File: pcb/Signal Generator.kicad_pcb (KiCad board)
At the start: 2 copper layers, 50 parts, among them J1 USB_C_Receptacle_USB2.0, J2 AudioJack3, J3 Conn_02x02_Odd_Even, J4 Screw_Terminal_01x04, SW1 SW_Push, SW2 SW_SPDT, U1 FT230XQ, U2 Opamp_Dual, U3 STM32F071RBTx, U4 LD39050PU33R, Y1 TG2520SMN_16.0000M-MCGNNM0

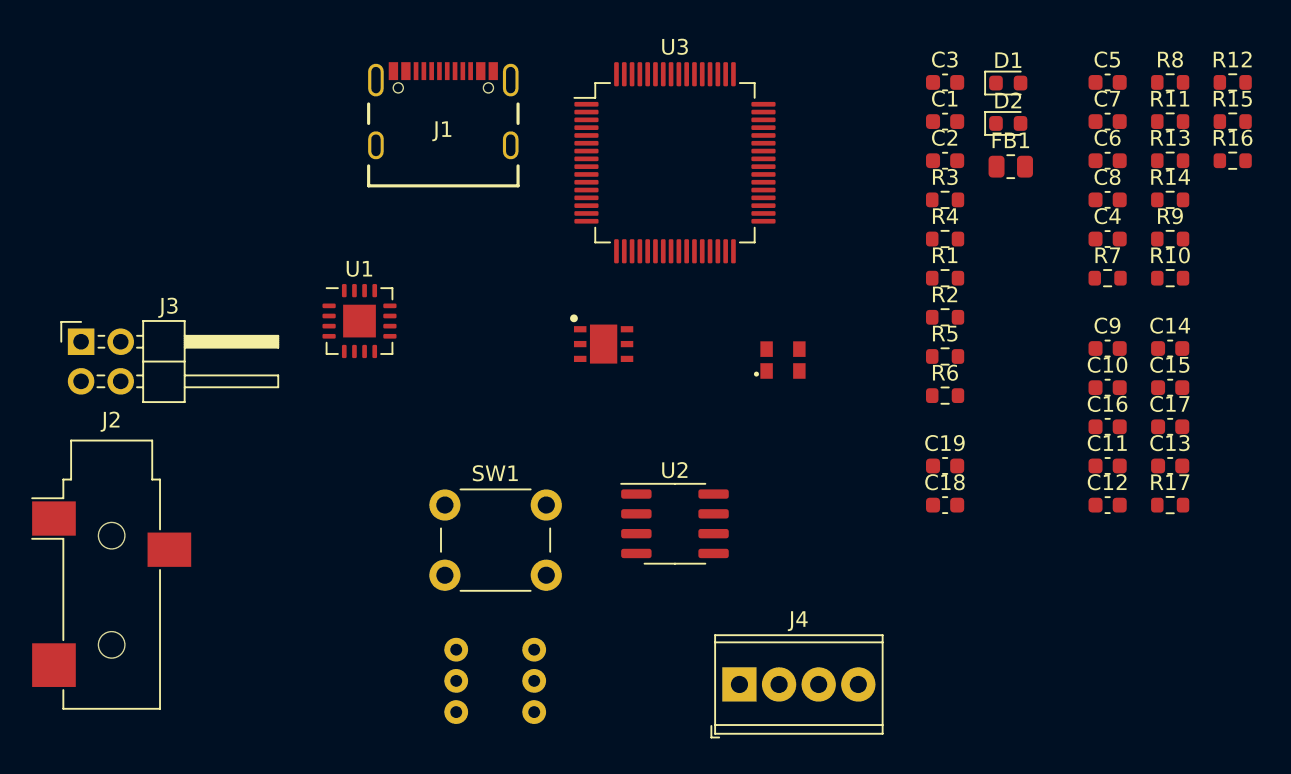
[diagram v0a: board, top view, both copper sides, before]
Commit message: Completed schematic oranization and components connection
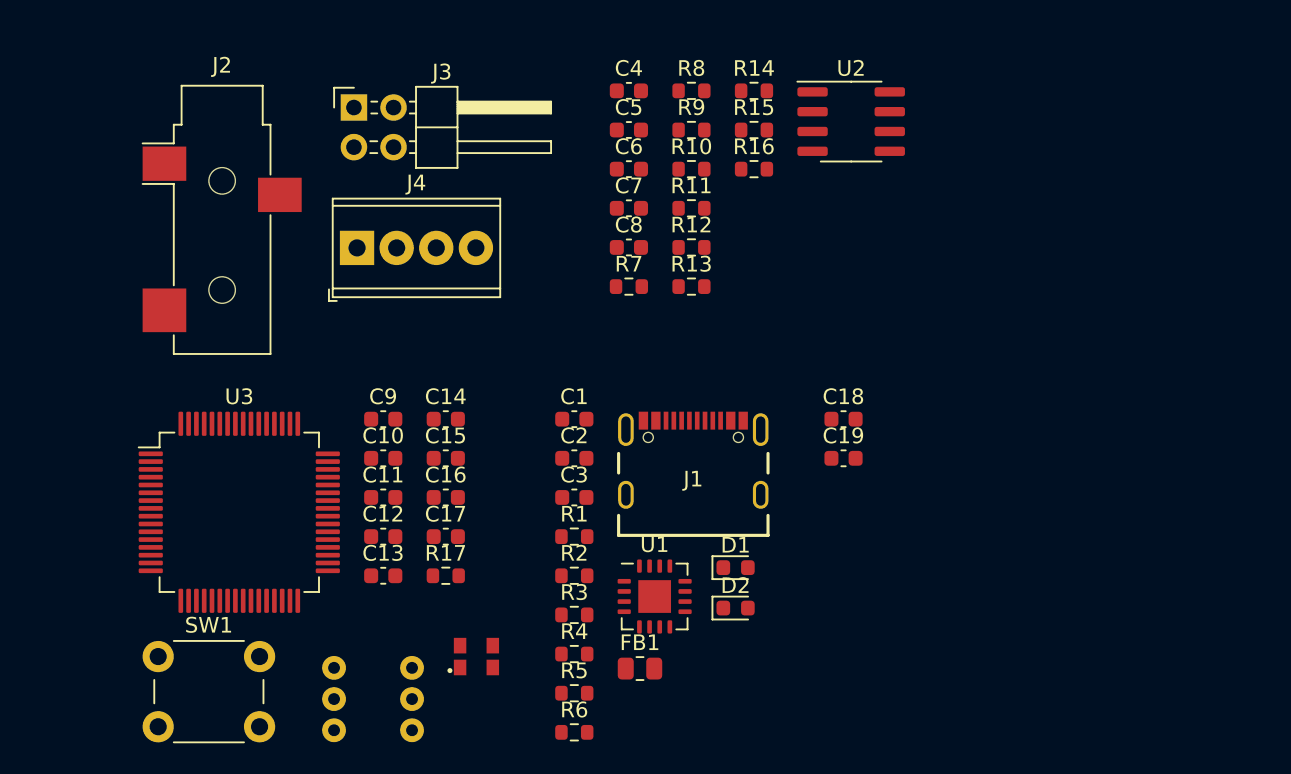
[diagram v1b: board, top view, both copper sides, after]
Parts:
- removed U4: LD39050PU33R, Signal Generator Components:LD39050PU33R
- moved C13 50.9 mm to (134.7, 118.9)
- moved C17 47.0 mm to (138.7, 116.4)
- moved C14 46.7 mm to (138.7, 108.9)
- moved C15 46.7 mm to (138.7, 111.4)
- moved R17 46.7 mm to (138.7, 118.9)
- moved C10 46.7 mm to (134.7, 111.4)
- moved C9 46.7 mm to (134.7, 108.9)
- moved C11 46.5 mm to (134.7, 113.9)
- moved C12 46.5 mm to (134.7, 116.4)
- moved C16 42.7 mm to (138.7, 113.9)
- moved FB1 40.0 mm to (151.2, 124.9)
- moved J4 37.2 mm to (133.0, 97.9)
- moved R12 36.3 mm to (154.5, 97.9)
- moved U3 35.8 mm to (125.5, 114.9)
- moved C3 35.7 mm to (147.0, 113.9)
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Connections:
- net +5V renamed /USB Connector/5V_USB
- net /MCU/OSC_IN renamed /MCU/OSC
- C19 pad 2: /Power/3V3 -> +3.3V
- U1 pad 15: /UART1_TX -> /MCU/UART1_TX
- U1 pad 2: /UART1_RX -> /MCU/UART1_RX
- U3 pad 13: unconnected-(U3-VDDA-Pad13) -> +3.3V
- U3 pad 15: /MCU/ADC1 -> /ADC1
- U3 pad 16: /MCU/ADC2 -> /ADC2
- U3 pad 21: /MCU/DAC1 -> /DAC1
- U3 pad 22: /MCU/DAC2 -> /DAC2
- U3 pad 60: unconnected-(U3-BOOT0-Pad60) -> /MCU/BOOT0
- U3 pad 7: unconnected-(U3-NRST-Pad7) -> /MCU/NRST

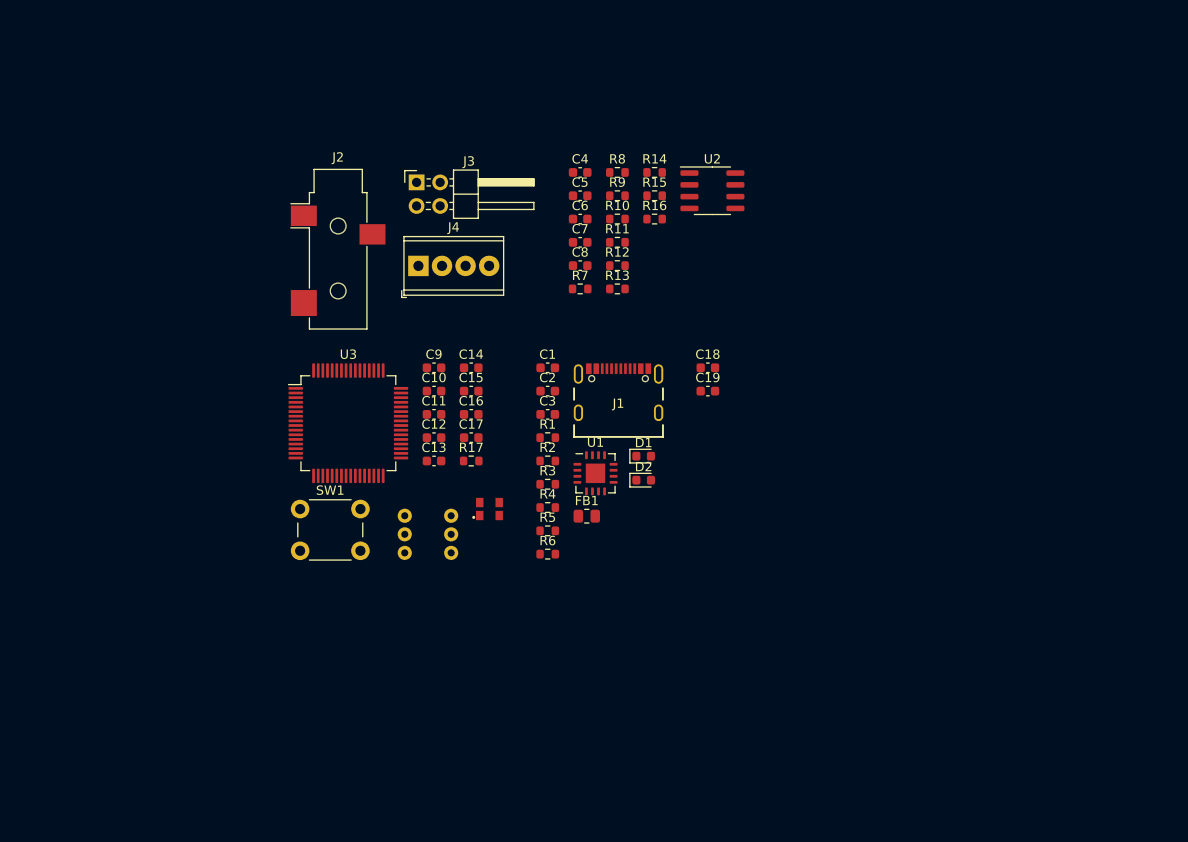
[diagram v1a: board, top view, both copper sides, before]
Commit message: Added micro SD and RGB led to schematic. Also added components part numbers
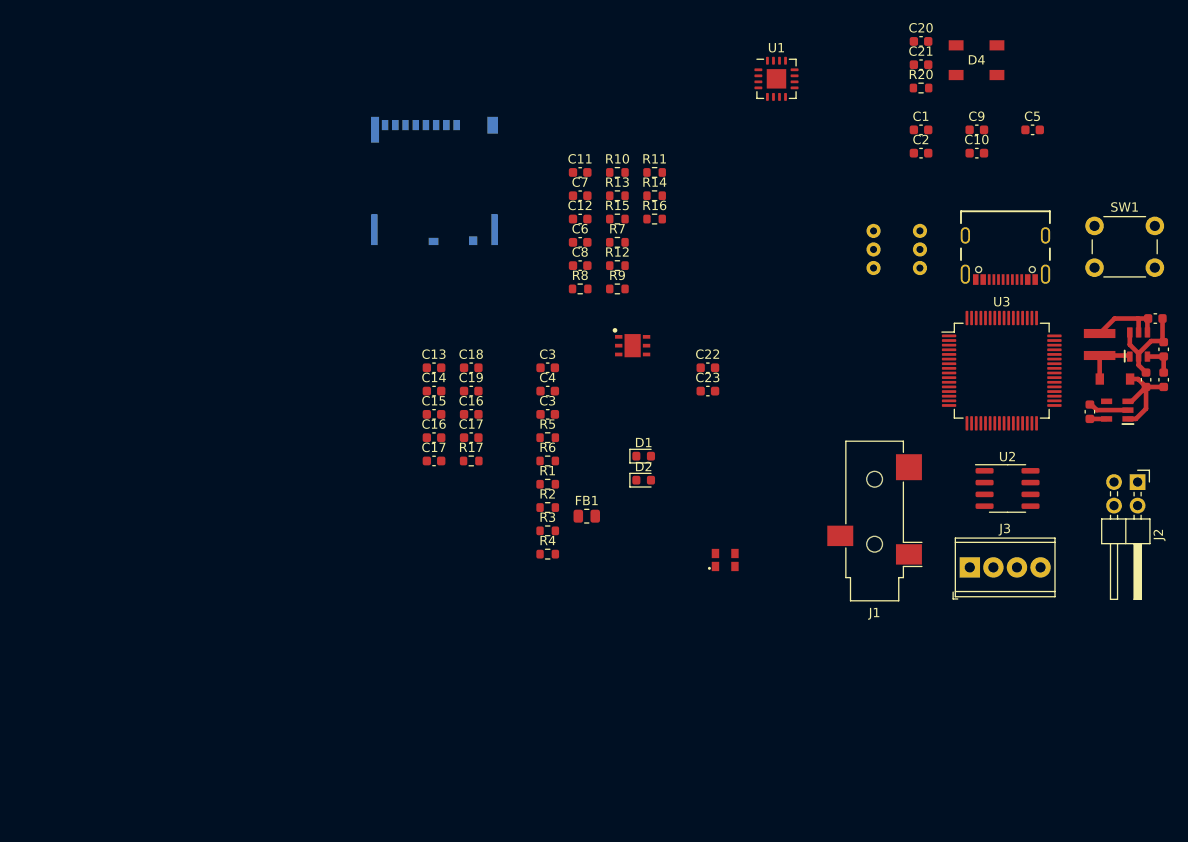
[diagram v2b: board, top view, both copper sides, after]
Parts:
- removed the J1 at (154.6, 113.7)
- added C1: 10u, Capacitor_SMD:C_0603_1608Metric, F.Cu at (187.2, 83.2)
- added C10: 100n, Capacitor_SMD:C_0603_1608Metric, F.Cu at (193.2, 85.8)
- added C2: 100n, Capacitor_SMD:C_0603_1608Metric, F.Cu at (187.2, 85.8)
- added C20: 4.7u, Capacitor_SMD:C_0603_1608Metric, F.Cu at (187.2, 73.7)
- added C21: 100n, Capacitor_SMD:C_0603_1608Metric, F.Cu at (187.2, 76.2)
- added C24: 1u, Capacitor_SMD:C_0603_1608Metric, F.Cu at (212.4, 103.6)
- added C25: 10u, Capacitor_SMD:C_0603_1608Metric, F.Cu at (211.4, 110.2)
- added C26: 1u, Capacitor_SMD:C_0603_1608Metric, F.Cu at (205.4, 113.6)
- added C5: 100n, Capacitor_SMD:C_0603_1608Metric, F.Cu at (199.2, 83.2)
- added C9: 100p, Capacitor_SMD:C_0603_1608Metric, F.Cu at (193.2, 83.2)
- added D3: D_Zener, Signal Generator Components:BZT52C10-TP, F.Cu at (208.1, 110.1)
- added D4: IN-PI55QA, Signal Generator Components:IN-PI55QA, F.Cu at (193.2, 75.7)
- added J4: MEM2080-00-128-00-A, Signal Generator Components:MEM2080-00-128-00-A, B.Cu at (134.8, 88.3)
- added J5: USB_C_Receptacle_USB2.0, Signal Generator Components:USB4105-GF-A, F.Cu at (196.3, 94.6)
- added L1: 4.7u, Signal Generator Components:XAL4030, F.Cu at (206.4, 106.4)
- added R18: 1.54M, Capacitor_SMD:C_0603_1608Metric, F.Cu at (213.3, 110.2)
- added R19: 100k, Capacitor_SMD:C_0603_1608Metric, F.Cu at (213.3, 106.9)
- added R20: 1k, Resistor_SMD:R_0603_1608Metric, F.Cu at (187.2, 78.7)
- added U4: LD39050PU33R, Signal Generator Components:LD39050PU33R, F.Cu at (156.1, 106.5)
- added U5: TLV61048, Signal Generator Components:TLV61048, F.Cu at (210.7, 106.4)
- added U6: LDK320AM120R, Signal Generator Components:LDK320AM120R, F.Cu at (208.3, 113.5)
- C11: renamed from C4; value C -> 6.8u
- C12: renamed from C6; value C -> 100n
- C13: renamed from C9; value C -> 10n
- C14: renamed from C10; value C -> 100n
- C15: renamed from C11; value C -> 100n
- C16: renamed from C12; value C -> 100n
- C17: renamed from C13; value C -> 100n
- C18: renamed from C14; value C -> 1u
- C19: renamed from C15; value C -> 4.7u
- C22: renamed from C18; value C -> 1u
- C23: renamed from C19; value C -> 1u
- C3: renamed from C1; value C -> 47p
- C4: renamed from C2; value C -> 47p
- C6: renamed from C7; value C -> 5p
- C7: renamed from C5; value C -> 100n
- C8: value C -> 5p
- D1: value LED -> LED Blue
- D2: value LED -> LED Orange
- R1: renamed from R3; value R -> 5.1k
- R11: renamed from R14; value R -> 91k
- R14: renamed from R15; value R -> 240k
- R16: value R -> 91k
- R17: value R -> 10k
- R2: renamed from R4; value R -> 5.1k
- R3: renamed from R5; value R -> 3.32
- R4: renamed from R6; value R -> 43.2
- R5: renamed from R1; value R -> 27
- R6: renamed from R2; value R -> 27
- R9: renamed from R13; value R -> 240k
- moved SW1 90.9 mm to (205.9, 93.6)
- moved J2 84.1 mm to (210.5, 121.2), turned to -90 degrees
- moved U3 70.6 mm to (195.9, 109.2)
- moved J3 67.7 mm to (192.5, 130.4)
- moved J1 64.8 mm to (182.2, 125.4), turned to 180 degrees
- moved SW2 59.1 mm to (180.1, 92.1)
- moved U1 46.8 mm to (171.6, 77.8)
- moved U2 45.2 mm to (196.5, 121.9)
- moved Y1 26.0 mm to (166.1, 129.6)
- renumbered J2 to J1, J3 to J2, J4 to J3, R8 to R10, R9 to R13, R10 to R15, R11 to R7, R7 to R8
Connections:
- net /USB Connector/5V_USB renamed /USB Connector/5V
- C17 pad 1: GND -> +3.3V
- C17 pad 2: +3.3V -> GND
- C23 pad 1: GND -> +3.3V
- C23 pad 2: +3.3V -> GND
- R3 pad 1: /USB Connector/FT_3V3 -> +3.3V
- R4 pad 1: /USB Connector/FT_3V3 -> Net-(D2-A)
- R4 pad 2: Net-(D2-A) -> +3.3V
- U3 pad 36: unconnected-(U3-PB15-Pad36) -> /MCU/LED_DIN
- U3 pad 50: unconnected-(U3-PA15-Pad50) -> /SD_CS
- U3 pad 55: unconnected-(U3-PB3-Pad55) -> /SD_SCK
- U3 pad 56: unconnected-(U3-PB4-Pad56) -> /SD_MISO
- U3 pad 57: unconnected-(U3-PB5-Pad57) -> /SD_MOSI
- U3 pad 58: unconnected-(U3-PB6-Pad58) -> /SD_Detect
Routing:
- net GND: track 0.00 -> 15.0 mm
- net /Power/13.12V: track 0.00 -> 11.3 mm
- net /USB Connector/5V: track 0.00 -> 8.97 mm
- net Net-(D3-A): track 0.00 -> 5.84 mm
- net Net-(U5-FB): track 0.00 -> 3.34 mm
- net +12VA: track 0.00 -> 1.80 mm

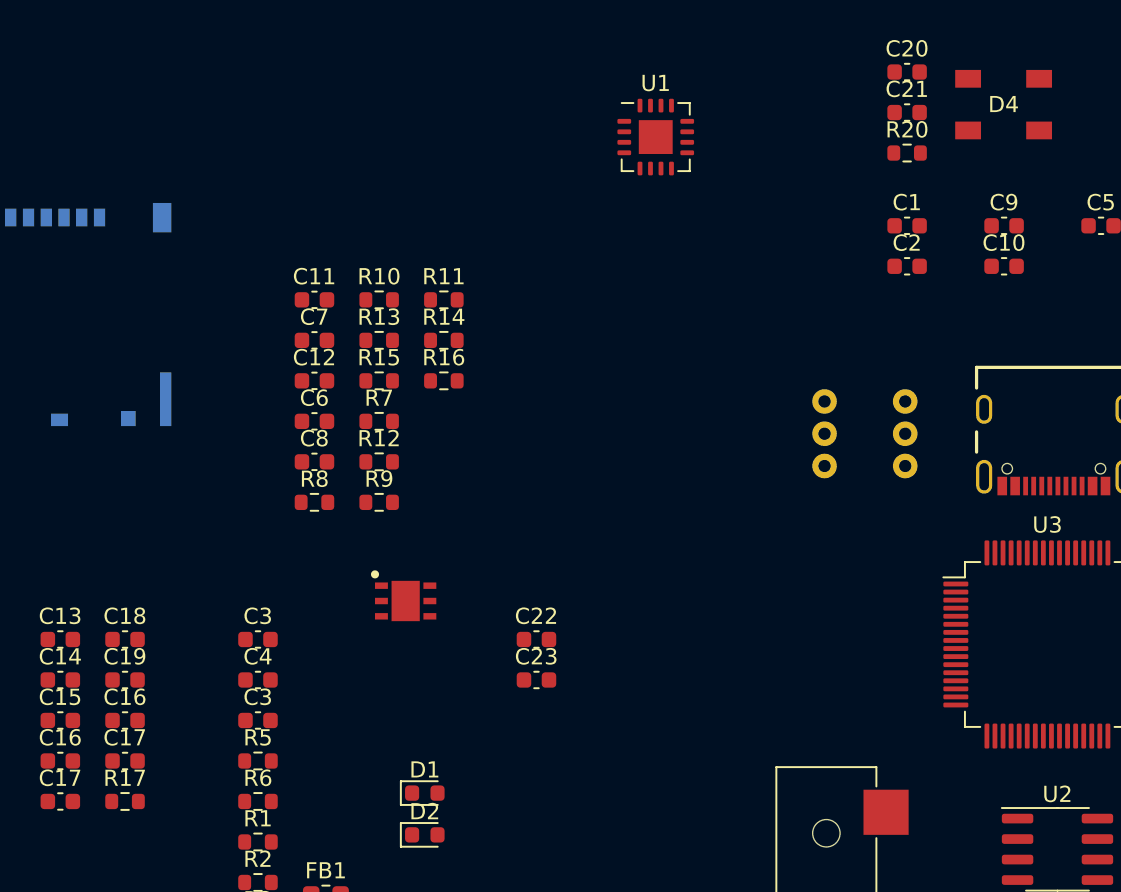
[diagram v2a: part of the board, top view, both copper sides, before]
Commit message: Added ST-Link connector to schematic
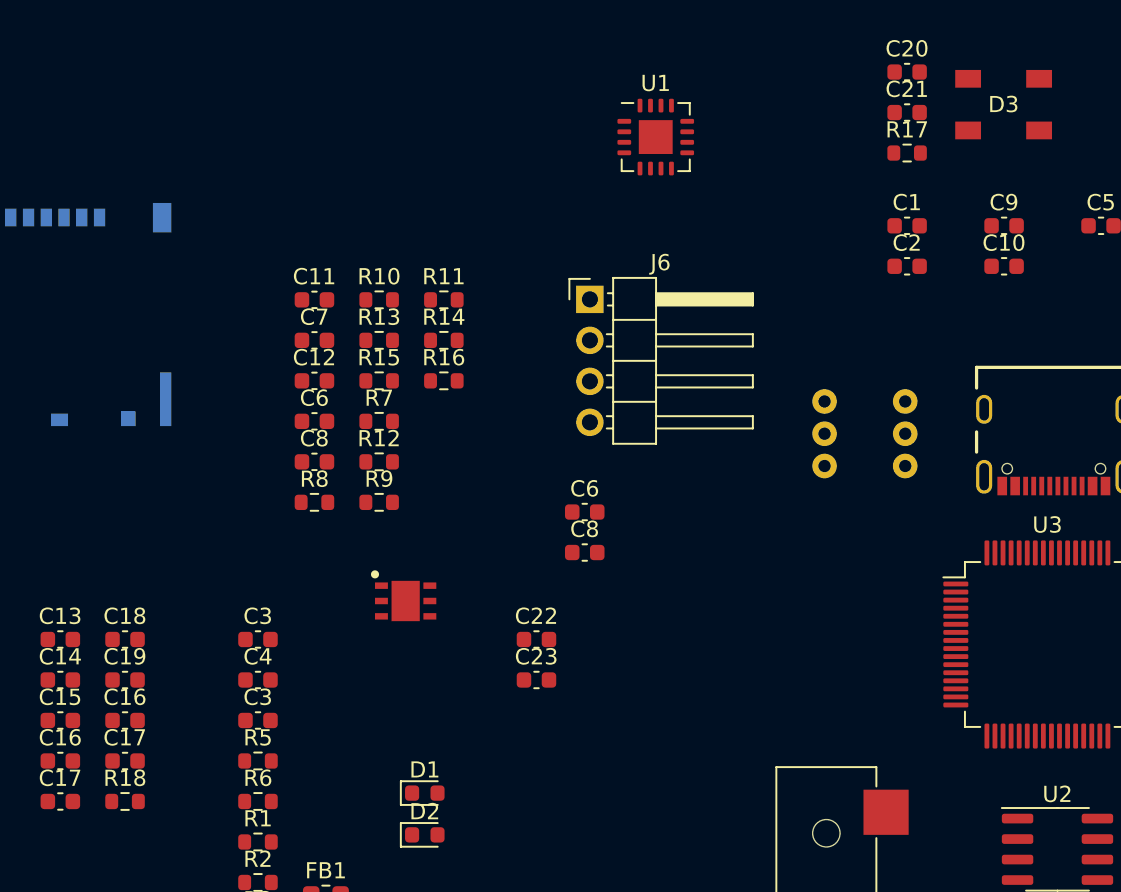
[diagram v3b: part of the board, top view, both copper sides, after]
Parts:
- added C6: 0.5p, Capacitor_SMD:C_0603_1608Metric, F.Cu at (167.2, 101.0)
- added C8: 0.5p, Capacitor_SMD:C_0603_1608Metric, F.Cu at (167.2, 103.5)
- added J6: Conn_01x04, Connector_PinHeader_2.54mm:PinHeader_1x04_P2.54mm_Horizontal, F.Cu at (167.5, 87.8)
- R10, R15: value R -> 1.33k
- R12, R7: value R -> 46.4k
- R13, R8: value R -> 4.75k
- renumbered D4 to D3, D3 to D4, R20 to R17, R17 to R18, R18 to R19, R19 to R20
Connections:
- C22 pad 1: /USB Connector/5V -> +5V
- C24 pad 1: /USB Connector/5V -> +5V
- L1 pad 1: /USB Connector/5V -> +5V
- U1 pad 10: /USB Connector/5V -> +5V
- U3 pad 34: unconnected-(U3-PB13-Pad34) -> /MCU/SWDIO
- U3 pad 35: unconnected-(U3-PB14-Pad35) -> /MCU/SWCLK
- U4 pad 1: /USB Connector/5V -> +5V
- U4 pad 6: /USB Connector/5V -> +5V
- U5 pad 4: /USB Connector/5V -> +5V
- U5 pad 5: /USB Connector/5V -> +5V
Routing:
- net /USB Connector/5V: track 8.97 -> 0.00 mm
- net +5V: track 0.00 -> 8.97 mm
